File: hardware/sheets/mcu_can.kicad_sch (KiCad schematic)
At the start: 36 parts, among them J2 Prog/UART, Q2 MMBT3904, Q3 MMBT3904, SW1 BOOT, SW2 EN/RESET, U5 ESP32-WROOM-32E-N8, U6 TJA1042T/3

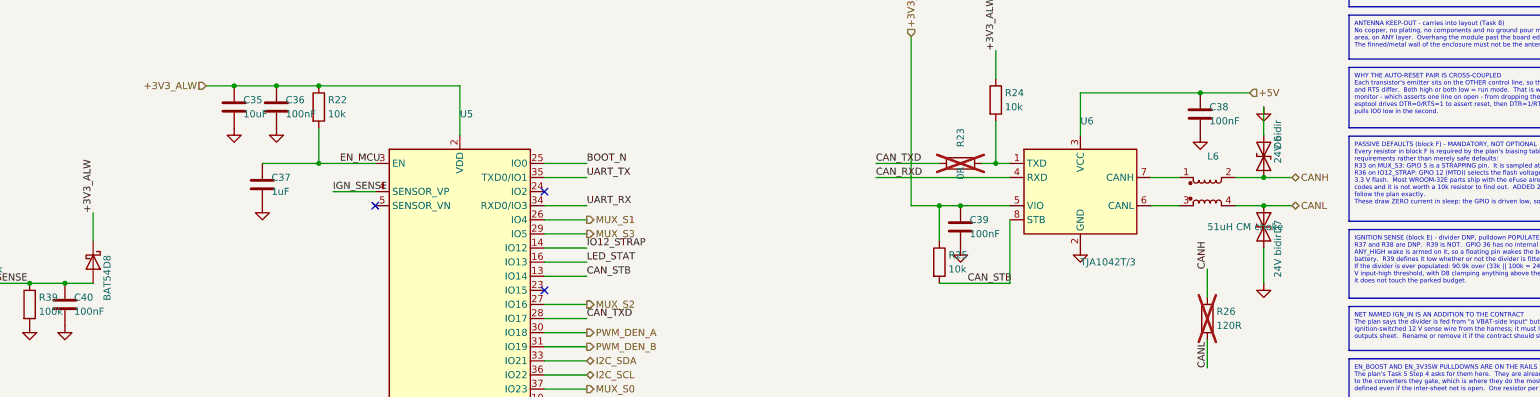
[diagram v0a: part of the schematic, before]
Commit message: hw(sch): sweep every selected part into the schematic; D6+D7 become one PESD2CANFD24U-T
Closes the gap the Task 7 review's finding F1 was about: parts chosen in
prose had not reached the generators, which is exactly how the superseded
SQJ415EP survived five days in the schematic.

STRUCTURAL - the CAN ESD pair is now one part. D6 and D7 were two placeholder
"24V bidir" discretes; the Nexperia PESD2CANFD24U-T is a single SOT23 holding
both bidirectional elements (K1/K2/CC). New verified symbol in symlib.py built
from Table 2 of the datasheet, added to gen_mcu_can's lib_symbols, and
Device:D_TVS dropped from that sheet since D6/D7 were its only users.

The two protected pins land exactly on the CANH and CANL runs, so each run is
drawn as TWO segments meeting AT the pin rather than one segment the pin
happens to touch. A pin sitting mid-wire does connect, but this project has
already produced one silent connectivity defect of that shape (labels
mid-wire, 14 instances), so the pin is made a wire endpoint and junctioned.
Verified from the netlist rather than from ERC: D6.1 -> /CANH, D6.2 -> /CANL,
D6.3 -> GND.

Consolidating freed D7, so the diode series was renumbered to stay gapless:
the ignition-divider BAT54 D8 -> D7, the twelve RGB sense clamps D9-D20 ->
D8-D19, and the PROFET sense clamp D21 -> D20. Every designator series is
gapless: C1-61, D1-20, F1-5, J1-8, L1-6, Q1-9, R1-99, SW1-2, U1-9.

VALUE SWEEP - L4/L5 "22uH" -> XAL7070-223ME, L6 "51uH CM choke" ->
ACT45B-510-2P-TL003, C3 "220uF" -> "220uF 63V" (the SMBJ24A's 8/20 us clamp is
50.6 V, so a 50 V part has no margin), U7 -> PCA9685PW/Q900, the only
AEC-Q100 variant in the ordering table. U7's lib_id stays Driver_LED:PCA9685PW
- that is the stock symbol's name, and the package is the same TSSOP28. D4 was
already SS5PH102.

FOOTPRINT - installed the vendor SamacSys footprint and STEP model for the
Wurth choke as footprints/mccan.pretty/Wurth_WE-CMBNC_7448031002.kicad_mod and
3dmodels/. Its pads verify against t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
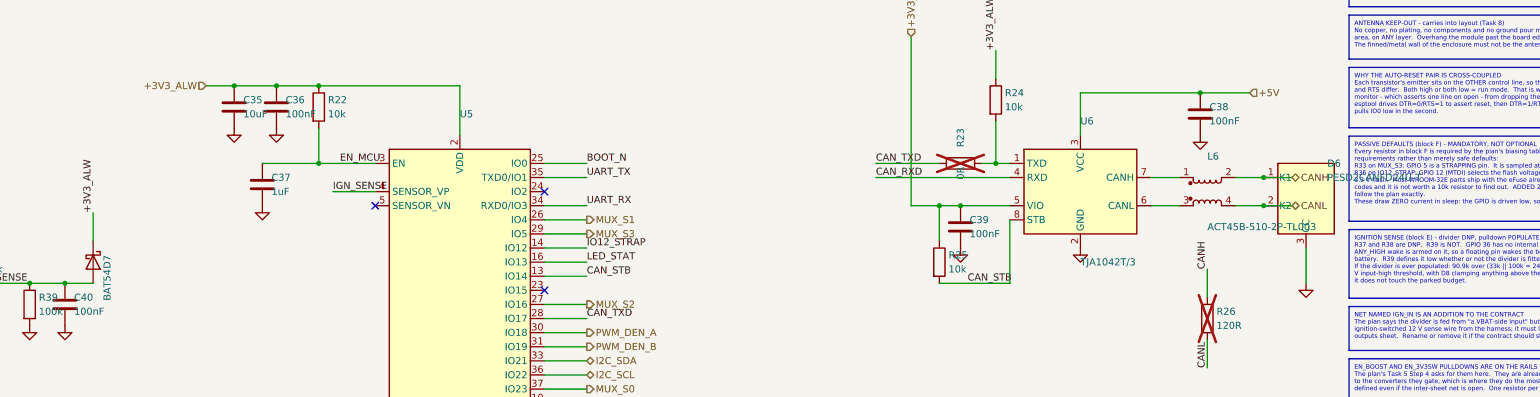
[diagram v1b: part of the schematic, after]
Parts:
- removed D8: BAT54, symbol Device:D_Schottky
- D6: value 24V bidir -> PESD2CANFD24U-T; symbol Device:D_TVS -> mccan_parts:PESD2CANFD24U
- D7: value 24V bidir -> BAT54; symbol Device:D_TVS -> Device:D_Schottky
- L6: value 51uH CM choke -> ACT45B-510-2P-TL003
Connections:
- net +3V3_ALW: now also D7.1 (K)
- net CANL: now also D6.2 (K2); no longer D7.1 (A1)
- net GND: now also D6.3 (CC); no longer D6.2 (A2), D7.2 (A2)
- net IGN_SENSE: now also D7.2 (A)
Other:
- moved on the sheet: D7

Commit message: hw(pcb): Task 8 step 0 - footprints assigned, 209 of 219 verified
Nothing in the project had a footprint except the PROFET's. Assignment now
lives in one auditable place, scripts/fpmap.py, which the four sheet
generators call when emitting each symbol's Footprint property. No generator
chooses a footprint of its own any more.

Three rules, and the reasoning is in the file rather than in a commit nobody
will read again: signal passives are 0603; a passive gets a bigger package
only for a stated reason; and nothing gets a footprint that has not been
checked to exist.

The reasons that drove a larger package:
- R2/R3, the 0R links bypassing the input choke windings, are 2512. They are
  DNP, but if anyone fits them for the tied-ground prototype they carry the
  entire 7.0 A night load, and a 0603 link is rated about 1 A.
- R52-R63, the RGB sense shunts, are 1206 for the FAULT case, not the normal
  7 mW. The package is sized on the understanding that firmware latches a
  shorted channel off; if that is ever dropped they must become 2512 1 W.
- The front-end ceramics are sized against the SMBJ24A's 8/20 us clamp of
  50.6 V, not the 38.9 V the distributor summaries quote. 100 nF fits 0805 at
  100 V; 1-2.2 uF at 63 V does not fit 0805; 10 uF at 63 V needs 1210.
- C20-C22 on +24 V are 1206 for DC-BIAS derating, a different reason - a 25 V
  X7R at 24 V keeps only 40-60% of nameplate.

Package identifications read from the datasheets rather than assumed:
NX5020UNBKS is SOT363/SC-88 (section 1), LM51571-Q1 RTE is WQFN-16 3x3 with a
1.66 mm exposed pad (so KiCad's EP1.675x1.675 is within tolerance), SS5PH102
is TO-277A, PESD2CANFD24U-T is SOT23.

FLAGGED, not silently accepted: the LM5164 DDA thermal pad is 3.4 x 2.8 mm on
the mechanical drawing and KiCad has no exact match. EP2.62x3.51 is the
closest by area (9.20 mm2 against 9.52) and is used for now, but that pad is
the part's heatsink on a thermally critical rail, so an exact DDA land pattern
should be drawn before fabr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
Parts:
- C35, C36, C37, C38, C39, C40: footprint (none) -> Capacitor_SMD:C_0603_1608Metric
- D5: footprint (none) -> LED_SMD:LED_0603_1608Metric
- D6, Q2, Q3: footprint (none) -> Package_TO_SOT_SMD:SOT-23
- D7: footprint (none) -> Diode_SMD:D_SOD-123
- J2: footprint (none) -> Connector_PinHeader_2.54mm:PinHeader_1x06_P2.54mm_Vertical
- R22, R23, R24, R25, R26, R27, R28, R29, R30, R31, R32, R33, R34, R35, R36, R37, R38, R39: footprint (none) -> Resistor_SMD:R_0603_1608Metric
- SW1, SW2: footprint (none) -> Button_Switch_SMD:Panasonic_EVQPUJ_EVQPUA
- U5: footprint (none) -> RF_Module:ESP32-WROOM-32E
- U6: footprint (none) -> Package_SO:SOIC-8_3.9x4.9mm_P1.27mm
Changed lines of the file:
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@@
 			)
 		)
-		(property "Footprint" ""
+		(property "Footprint" "RF_Module:ESP32-WROOM-32E"
 			(at 149.86 120.65 0)
 			(hide yes)
@@
 			)
 		)
-		(property "Footprint" ""
+		(property "Footprint" "Resistor_SMD:R_0603_1608Metric"
 			(at 60.96 107.95 0)
 			(hide yes)
@@
 			)
 		)
-		(property "Footprint" ""
+		(property "Footprint" "Capacitor_SMD:C_0603_1608Metric"
 			(at 116.84 80.01 0)
 			(hide yes)
@@
 			)
 		)
-		(property "Footprint" ""
+		(property "Footprint" "Resistor_SMD:R_0603_1608Metric"
 			(at 55.88 224.79 0)
 			(hide yes)
@@
 			)
 		)
-		(property "Footprint" ""
+		(property "Footprint" "Resistor_SMD:R_0603_1608Metric"
 			(at 71.12 224.79 0)
 			(hide yes)
@@
 			)
 		)
-		(property "Footprint" ""
+		(property "Footprint" "Resistor_SMD:R_0603_1608Metric"
 			(at 40.64 224.79 0)
 			(hide yes)
@@
 			)
 		)
-		(property "Footprint" ""
+		(property "Footprint" "Capacitor_SMD:C_0603_1608Metric"
 			(at 78.74 115.57 0)
 			(hide yes)
@@
 			)
 		)
-		(property "Footprint" ""
+		(property "Footprint" "Capacitor_SMD:C_0603_1608Metric"
 			(at 283.21 81.28 0)
 			(hide yes)
@@
 			)
 		)
-		(property "Footprint" ""
+		(property "Footprint" "Diode_SMD:D_SOD-123"
 			(at 83.82 107.95 0)
 			(hide yes)
@@
 			)
 		)
-		(property "Footprint" ""
+		(property "Footprint" "Resistor_SMD:R_0603_1608Metric"
 			(at 240.03 90.17 0)
 			(hide yes)
@@
 			)
 		)
-		(property "Footprint" ""
+		(property "Footprint" "Resistor_SMD:R_0603_1608Metric"
 			(at 132.08 224.79 0)
 			(hide yes)
@@
 			)
 		)
-		(property "Footprint" ""
+		(property "Footprint" "Capacitor_SMD:C_0603_1608Metric"
 			(at 109.22 80.01 0)
 			(hide yes)
@@
 			)
 		)
-		(property "Footprint" ""
+		(property "Footprint" "Resistor_SMD:R_0603_1608Metric"
 			(at 72.39 170.18 0)
 			(hide yes)
@@
 			)
 		)
-		(property "Footprint" ""
+		(property "Footprint" "Capacitor_SMD:C_0603_1608Metric"
 			(at 114.3 93.98 0)
 			(hide yes)
@@
 			)
 		)
-		(property "Footprint" ""
+		(property "Footprint" "Resistor_SMD:R_0603_1608Metric"
 			(at 246.38 78.74 0)
 			(hide yes)
@@
 			)
 		)
-		(property "Footprint" ""
+		(property "Footprint" "Capacitor_SMD:C_0603_1608Metric"
 			(at 240.03 101.6 0)
 			(hide yes)
@@
 			)
 		)
-		(property "Footprint" ""
+		(property "Footprint" "Resistor_SMD:R_0603_1608Metric"
 			(at 72.39 115.57 0)
 			(hide yes)
@@
 			)
 		)
-		(property "Footprint" ""
+		(property "Footprint" "Button_Switch_SMD:Panasonic_EVQPUJ_EVQPUA"
 			(at 110.49 158.75 0)
 			(hide yes)
@@
 			)
 		)
-		(property "Footprint" ""
+		(property "Footprint" "Package_TO_SOT_SMD:SOT-23"
 			(at 302.26 95.25 0)
 			(hide yes)
@@
 			)
 		)
-		(property "Footprint" ""
+		(property "Footprint" "Package_TO_SOT_SMD:SOT-23"
 			(at 85.09 170.18 0)
 			(hide yes)
@@
 			)
 		)
-		(property "Footprint" ""
+		(property "Footprint" "Package_TO_SOT_SMD:SOT-23"
 			(at 85.09 189.23 0)
 			(hide yes)
@@
 			)
 		)
-		(property "Footprint" ""
+		(property "Footprint" "Button_Switch_SMD:Panasonic_EVQPUJ_EVQPUA"
 			(at 110.49 204.47 0)
 			(hide yes)
@@
 			)
 		)
-		(property "Footprint" ""
+		(property "Footprint" "Resistor_SMD:R_0603_1608Metric"
 			(at 124.46 80.01 0)
 			(hide yes)
@@
 			)
 		)
-		(property "Footprint" ""
+		(property "Footprint" "Resistor_SMD:R_0603_1608Metric"
 			(at 236.22 107.95 0)
 			(hide yes)
@@
 			)
 		)
-		(property "Footprint" ""
+		(property "Footprint" "Resistor_SMD:R_0603_1608Metric"
 			(at 116.84 224.79 0)
 			(hide yes)
@@
 			)
 		)
-		(property "Footprint" ""
+		(property "Footprint" "Resistor_SMD:R_0603_1608Metric"
 			(at 220.98 160.02 0)
 			(hide yes)
@@
 			)
 		)
-		(property "Footprint" ""
+		(property "Footprint" "Resistor_SMD:R_0603_1608Metric"
 			(at 72.39 189.23 0)
 			(hide yes)
@@
 			)
 		)
-		(property "Footprint" ""
+		(property "Footprint" "LED_SMD:LED_0603_1608Metric"
 			(at 209.55 160.02 0)
 			(hide yes)
@@
 			)
 		)
-		(property "Footprint" ""
+		(property "Footprint" "Resistor_SMD:R_0603_1608Metric"
 			(at 101.6 224.79 0)
 			(hide yes)
@@
 			)
 		)
-		(property "Footprint" ""
+		(property "Footprint" "Resistor_SMD:R_0603_1608Metric"
 			(at 60.96 115.57 0)
 			(hide yes)
@@
 			)
 		)
-		(property "Footprint" ""
+		(property "Footprint" "Resistor_SMD:R_0603_1608Metric"
 			(at 86.36 224.79 0)
 			(hide yes)
@@
 			)
 		)
-		(property "Footprint" ""
+		(property "Footprint" "Connector_PinHeader_2.54mm:PinHeader_1x06_P2.54mm_Vertical"
 			(at 60.96 175.26 0)
 			(hide yes)
@@
 			)
 		)
-		(property "Footprint" ""
+		(property "Footprint" "Resistor_SMD:R_0603_1608Metric"
 			(at 284.48 118.11 0)
 			(hide yes)
@@
 			)
 		)
-		(property "Footprint" ""
+		(property "Footprint" "Package_SO:SOIC-8_3.9x4.9mm_P1.27mm"
 			(at 261.62 95.25 0)
 			(hide yes)

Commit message: hw(sch): CM chokes were wired to KiCad's pin numbering, not the parts'
Both common-mode chokes used Device:L_Coupled, which numbers its pins
winding A = 1-2, winding B = 3-4.  Every real four-terminal CM choke numbers
them winding A = 1-4, winding B = 2-3.  Both parts in this design are real
ones, so both were wired across the wrong pairs.

L2 was the serious one.  As drawn, winding 1-4 tied VBAT_PROT to board GND
and winding 2-3 tied VBAT_F to GND_IN -- two dead shorts across the supply
through 6.3 mOhm windings.  First power-up would have cleared the 10 A fuse
with the P-FET and the choke carrying the fault.

L6 transposed CANH and CANL between the transceiver and the connector, so the
board would never have received a frame.  Being listen-only by default, the
symptom is "no traffic" -- which spec 8.3 already names as the top risk and
the thing most likely to be misdiagnosed as a firmware fault.

ERC passes either way.  DRC passes either way.  The footprint pad count
matches either way.  Nothing automated catches this.

Verified from the VECTOR GEOMETRY of both datasheets, not a text dump -- a
flat extraction gives four bare numerals with no axis:
  Wurth WE-CMBNC 7448031002 "Schematic": upper coil's leads sit under labels
    1 (x=347.0) and 4 (x=488.6); lower coil's under 2 and 3 at the same x.
  TDK ACT45B "CIRCUIT DIAGRAM": identical, 1/4 upper, 2/3 lower.

Fix is a mccan_parts:CM_CHOKE_4T symbol drawn with L_Coupled's own graphics
but numbered to match the parts.  Not one wire moves -- which is also why the
drawing never looked wrong.  Netlist now reads:
  L2.1->4  VBAT_PROT -> VBAT_F      L2.2->3  GND_IN -> GND
  L6.1->4  U6 CANH   -> CANH        L6.2->3  U6 CANL -> CANL

Also in this commit, from the two datasheets supplied today:

- Superseal is a WIRE-TO-WIRE series with no panel-mount board-side housing,
  so the seven "panel connectors" could never have been built, and that is
  why all seven sat in fpmap.BLOCKED through Task 8 step 0.  J1 and J3-J8
  b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
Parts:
- L6: footprint (none) -> mccan:TDK_ACT45B; symbol Device:L_Coupled -> mccan_parts:CM_CHOKE_4T
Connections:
- net CANH: now also L6.4; no longer L6.2
- net CANL: now also L6.3; no longer L6.4
- net at U6.6 (CANL): now also L6.2; no longer L6.3
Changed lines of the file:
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@@
 	)
 	(symbol
-		(lib_id "Device:L_Coupled")
+		(lib_id "mccan_parts:CM_CHOKE_4T")
 		(at 284.48 95.25 0)
 		(unit 1)
@@
 			)
 		)
-		(property "Footprint" ""
+		(property "Footprint" "mccan:TDK_ACT45B"
 			(at 284.48 95.25 0)
 			(hide yes)
@@
 		(pin "1"
 		)
+		(pin "4"
+		)
 		(pin "2"
 		)
 		(pin "3"
 		)
-		(pin "4"
-		)
 		(instances

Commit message: hw(mcu): final GPIO map for twelve outputs, shared diagnostics and RTC CAN RX
Co-Authored-By: Claude Sonnet 5.5 <noreply@anthropic.com>
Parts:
- removed C40: 100nF, Capacitor_SMD:C_0603_1608Metric, symbol Device:C
- removed D7: BAT54, Diode_SMD:D_SOD-123, symbol Device:D_Schottky
- removed R23: 0R, Resistor_SMD:R_0603_1608Metric, symbol Device:R
- removed R34, R35: 10k, Resistor_SMD:R_0603_1608Metric, symbol Device:R
- removed R37: 90.9k, Resistor_SMD:R_0603_1608Metric, symbol Device:R
- removed R38: 33k, Resistor_SMD:R_0603_1608Metric, symbol Device:R
- removed R39: 100k, Resistor_SMD:R_0603_1608Metric, symbol Device:R
- R30, R31, R32: value 10k -> 4.7k
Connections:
- net GND: no longer R30.2, R31.2, R32.2
- net DIAG_SEL1: now reaches U5.23 (IO15)
- net DIAG_SEL1: now also R32.1
- net DIAG_EN: now reaches U5.24 (IO2)
- net DIAG_EN: now also R30.1
- net SNS_C: now reaches U5.5 (SENSOR_VN)
- net CAN_TXD renamed OUT_RL_BRK
- net DEN_DSEL renamed OUT_FR_IND
- net EN_3V3SW renamed OUT_FL_IND
- net EN_BOOST renamed OUT_FL_DRL
- net EN_DIAG renamed OUT_RL_DRL
- net I2C_SCL renamed OUT_AUX_L
- net I2C_SDA renamed OUT_RR_BRK
- net IGN_SENSE renamed SNS_B
- net ISNS_DEN renamed SNS_A
- net MUX_S0 renamed OUT_AUX_R
- net OUT_AUX_R: no longer R30.1
- net MUX_S1 renamed DIAG_SEL0
- net DIAG_SEL0: now also U5.29 (IO5); no longer U5.26 (IO4)
- net MUX_S2 renamed OUT_RL_IND
- net OUT_RL_IND: no longer R32.1
- net MUX_S3 renamed DIAG_EN_Q
- net DIAG_EN_Q: now also R30.2; no longer U5.29 (IO5)
- net PWM_DEN_A renamed OUT_RR_DRL
- net PWM_DEN_B renamed OUT_RR_IND
- net RGB_ISNS renamed OUT_FR_DRL
- new net DIAG_SEL0_Q: R31.2
- new net DIAG_SEL1_Q: R32.2
- new net EN_5V: U5.26 (IO4)
- no-connect marks 3 -> 7
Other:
- moved on the sheet: R30, R31, R32, R33

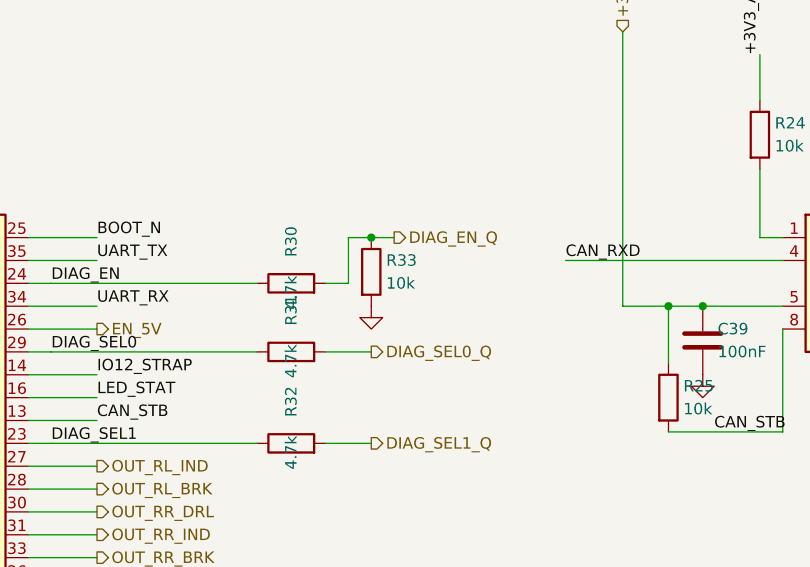
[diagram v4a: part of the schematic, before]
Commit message: fix: final-review wave: DIAG_EN margin, feed-B return before the choke, true protection claims
Co-Authored-By: Claude Opus 5.5 <noreply@anthropic.com>
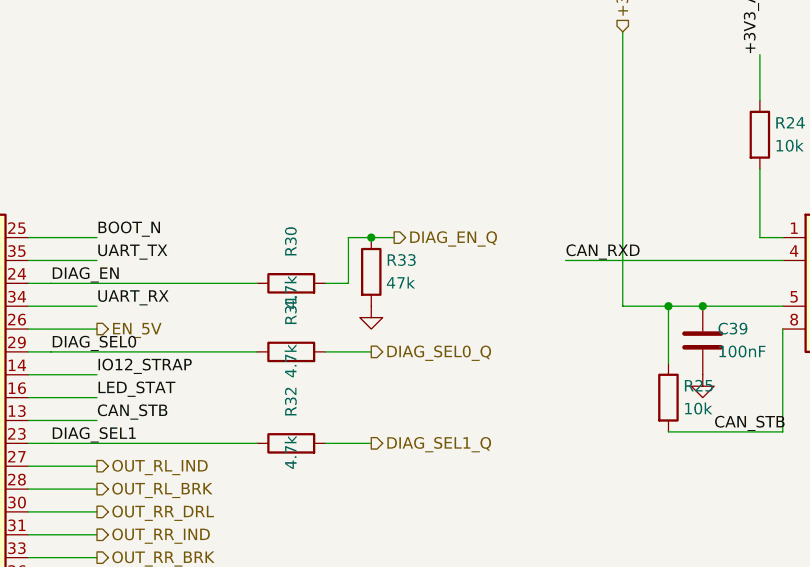
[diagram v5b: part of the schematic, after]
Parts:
- R33: value 10k -> 47k
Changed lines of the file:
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@@
 			)
 		)
-		(property "Value" "10k"
+		(property "Value" "47k"
 			(at 204.851 95.25 0)
 			(show_name no)
